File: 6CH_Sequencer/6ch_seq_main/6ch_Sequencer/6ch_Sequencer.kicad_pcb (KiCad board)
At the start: 2 copper layers, 30 x 99 mm, 38 parts, among them J1 CH1, J2 CH2, J3 CH3, J4 CH4, J5 CH5, J6 CH6, J7 CLOCK_IN, J8 POWER, SW1 SW_Push, SW2 Rotary_Encoder

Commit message: addMountingHole
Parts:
- added Mounting: MountingHole_3.2mm_M3, Mounting_Holes:MountingHole_3.2mm_M3, F.Cu at (79.2, 131.8)
- added Mounting: MountingHole_3.2mm_M3, Mounting_Holes:MountingHole_3.2mm_M3, F.Cu at (102.2, 46.5)
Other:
- board text added: "CH1"
- board text added: "CH2"
- board text added: "CH3"
- board text added: "CH4"
- board text added: "CH5"
- board text added: "CH6"
- board text added: "CLOCK IN"
- board text added: "Designed by HAGIWO Mar 2021 V.1.0"
- board text added: "GND"
- board text added: "SCL"
- board text added: "SDA"
- board text added: "VCC"

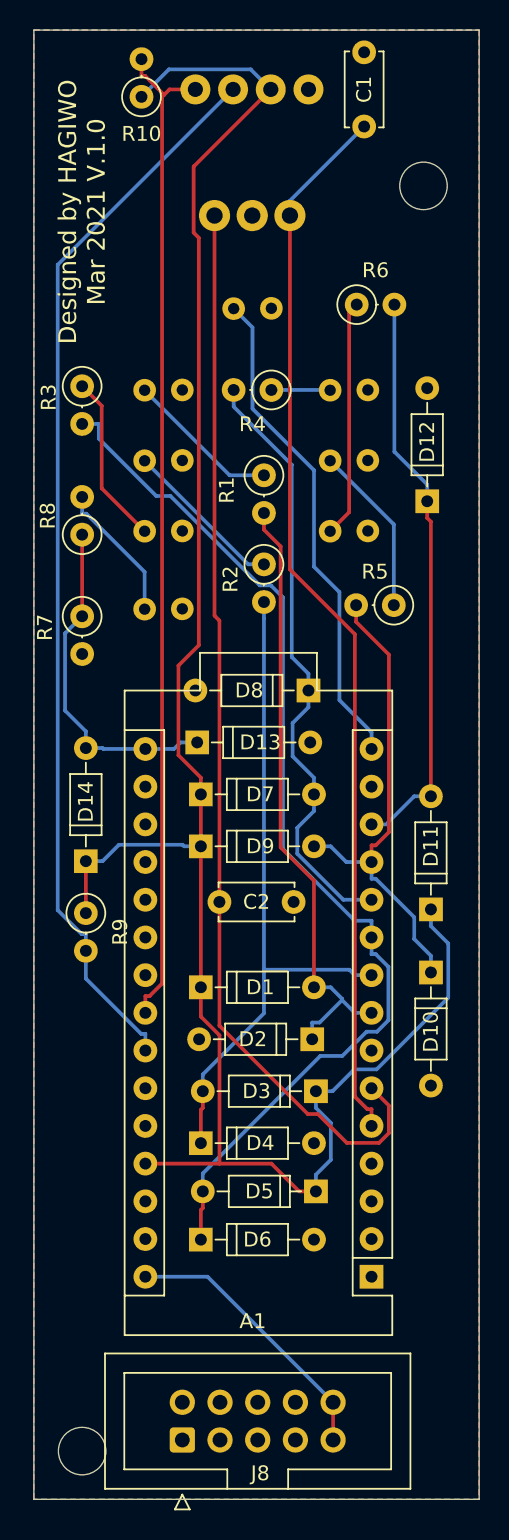
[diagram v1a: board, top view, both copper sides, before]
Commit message: AddControlPanel
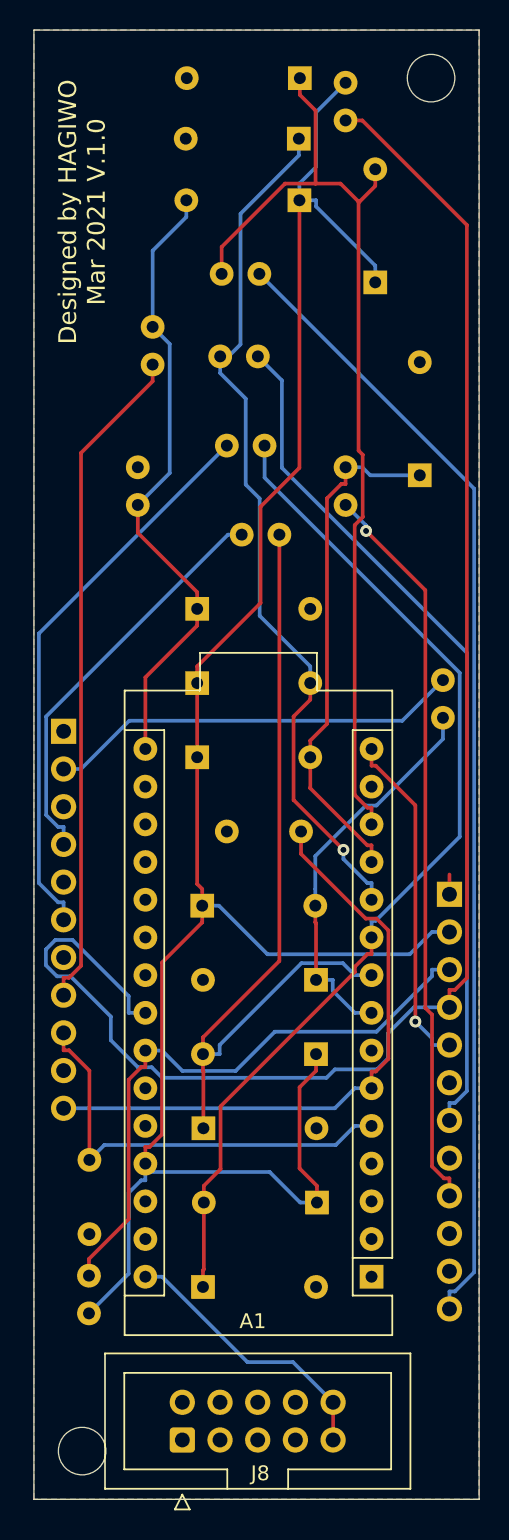
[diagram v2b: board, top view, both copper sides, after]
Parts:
- removed Brd1: SSD1306, digikey-footprints:PinHeader_1x4_P2.54mm_Drill1.02mm
- removed J1: CH1, digikey-footprints:PinHeader_1x2_P2.54mm
- removed J2: CH2, digikey-footprints:PinHeader_1x2_P2.54mm
- removed J3: CH3, digikey-footprints:PinHeader_1x2_P2.54mm
- removed J4: CH4, digikey-footprints:PinHeader_1x2_P2.54mm
- removed J5: CH5, digikey-footprints:PinHeader_1x2_P2.54mm
- removed J6: CH6, digikey-footprints:PinHeader_1x2_P2.54mm
- removed J7: CLOCK_IN, digikey-footprints:PinHeader_1x2_P2.54mm
- removed SW1: SW_Push, digikey-footprints:PinHeader_1x2_P2.54mm
- removed SW2: Rotary_Encoder, digikey-footprints:PinHeader_1x3_P2.54_Drill1.1mm
- added Conn1: Pin_Header_Straight_1x11_Pitch2.54mm, Pin_Headers:Pin_Header_Straight_1x11_Pitch2.54mm, B.Cu at (78.0, 83.2)
- added Conn2: Pin_Header_Straight_1x12_Pitch2.54mm, Pin_Headers:Pin_Header_Straight_1x12_Pitch2.54mm, B.Cu at (104.0, 94.2)
- C1, C2, D1, D10, D11, D12, D13, D14, D2, D3, D4, D5, D6, D7, D8, D9, R1, R10, R2, R3, R4, R5, R6, R7, R8, R9: moved to B.Cu
- moved C1 72.0 mm to (79.7, 112.1), turned to 270 degrees
- moved D14 46.8 mm to (93.9, 47.5), turned to 180 degrees
- moved D11 42.4 mm to (99.0, 53.0)
- moved D8 37.2 mm to (93.8, 43.3)
- moved D10 33.5 mm to (102.0, 66.0), turned to 90 degrees
- moved D12 29.8 mm to (93.9, 39.2), turned to 180 degrees
- moved R9 27.0 mm to (79.7, 122.5), turned to 90 degrees
- moved R1 18.3 mm to (103.6, 79.8)
- moved R8 14.8 mm to (84.0, 56.0), turned to 270 degrees
- moved R10 13.8 mm to (97.0, 39.5), turned to 270 degrees
- moved R3 10.5 mm to (89.0, 64.0), turned to 0 degrees
- moved D13 9.00 mm to (87.0, 75.0)
- moved R7 8.39 mm to (83.0, 68.0), turned to 90 degrees
- moved D7 7.50 mm to (87.0, 80.0)
- moved R5 7.49 mm to (97.0, 68.0), turned to 90 degrees
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- renumbered Mounting to Mounting1, Mounting to Mounting2
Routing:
- net Net-(J6-PadT): track 16.0 -> 76.6 mm
- net Net-(J4-PadT): track 3.97 -> 58.0 mm
- net Net-(A1-Pad5): track 71.9 -> 29.5 mm
- net Net-(A1-Pad23): track 68.0 -> 109.5 mm
- net Net-(J5-PadT): track 11.5 -> 49.7 mm, vias 0 -> 1
- net Net-(J7-PadT): track 9.47 -> 45.2 mm
- net Net-(A1-Pad24): track 72.4 -> 41.1 mm
- net Net-(A1-Pad6): track 73.2 -> 42.1 mm
- net Net-(A1-Pad13): track 39.0 -> 66.5 mm
- net Net-(J3-PadT): track 11.5 -> 38.1 mm
- net Net-(A1-Pad16): track 23.1 -> 42.4 mm
- net Net-(A1-Pad11): track 41.1 -> 59.4 mm, vias 0 -> 1
- net Net-(J1-PadT): track 10.4 -> 28.0 mm
- net Net-(J2-PadT): track 10.9 -> 27.6 mm
- net Net-(A1-Pad8): track 41.8 -> 26.7 mm
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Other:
- board text added: "J1 CH1"
- board text added: "J2 CH2"
- board text added: "J3 CH3"
- board text added: "J4 CH4"
- board text added: "J5 CH5"
- board text added: "J6 CH6"
- board text added: "SW1"
- board text added: "SW2"
- board text removed: "CH1"
- board text removed: "CH2"
- board text removed: "CH3"
- board text removed: "CH4"
- board text removed: "CH5"
- board text removed: "CH6"
